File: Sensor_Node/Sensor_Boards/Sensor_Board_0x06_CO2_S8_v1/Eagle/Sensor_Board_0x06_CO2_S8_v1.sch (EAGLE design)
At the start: 16 parts, among them J1 M04_SMD_90, J3 M03_SMD_90, J4 ARDUINO_ISP, U1 SENSEAIR_S8_SMD, U2 ATMEGA328P_TQFP, Y1 8MHZ

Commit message: Removed gap between connectors to commBoard, added power jack
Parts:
- added J2: 5.5x2.1mm Barrel, wsn:POWER_JACKSMD
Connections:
- net +5V: now also J2.PWR
- net GND: now also J2.GND, J2.GNDBREAK
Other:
- note added: "ATmega328p"
- note added: "Power Jack"
- note removed: "ATmega328"
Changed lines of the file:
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@@
 <?xml version="1.0" encoding="utf-8"?>
 <!DOCTYPE eagle SYSTEM "eagle.dtd">
-<eagle version="8.2.0">
+<eagle version="8.2.2">
 <drawing>
 <settings>
@@
 <layer number="115" name="ReferenceISLANDS" color="7" fill="1" visible="yes" active="yes"/>
 <layer number="116" name="Patch_BOT" color="9" fill="4" visible="yes" active="yes"/>
+<layer number="117" name="BACKMAAT1" color="7" fill="1" visible="yes" active="yes"/>
 <layer number="118" name="Rect_Pads" color="7" fill="1" visible="yes" active="yes"/>
+<layer number="119" name="KAP_TEKEN" color="7" fill="1" visible="yes" active="yes"/>
+<layer number="120" name="KAP_MAAT1" color="7" fill="1" visible="yes" active="yes"/>
 <layer number="121" name="_tsilk" color="7" fill="1" visible="yes" active="yes"/>
 <layer number="122" name="_bsilk" color="7" fill="1" visible="yes" active="yes"/>
@@
 <layer number="128" name="_bValues" color="7" fill="1" visible="yes" active="yes"/>
 <layer number="129" name="Mask" color="7" fill="1" visible="yes" active="yes"/>
+<layer number="130" name="SMDSTROOK" color="7" fill="1" visible="yes" active="yes"/>
 <layer number="131" name="tAdjust" color="7" fill="1" visible="yes" active="yes"/>
 <layer number="132" name="bAdjust" color="7" fill="1" visible="yes" active="yes"/>
+<layer number="133" name="bottom_silk" color="7" fill="1" visible="yes" active="yes"/>
 <layer number="144" name="Drill_legend" color="7" fill="1" visible="yes" active="yes"/>
 <layer number="150" name="Notes" color="7" fill="1" visible="yes" active="yes"/>
@@
 <part name="U$16" library="myownthings" deviceset="N/C" device=""/>
 <part name="U$17" library="myownthings" deviceset="N/C" device=""/>
+<part name="J2" library="wsn" deviceset="POWER_JACK" device="SMD" value="5.5x2.1mm Barrel"/>
+<part name="P+5" library="supply1" deviceset="+5V" device=""/>
+<part name="GND4" library="SparkFun" deviceset="GND" device=""/>
 </parts>
 <sheets>
@@
 <wire x1="124.46" y1="116.84" x2="124.46" y2="203.2" width="0.1524" layer="97" style="shortdash"/>
 <wire x1="124.46" y1="203.2" x2="7.62" y2="203.2" width="0.1524" layer="97" style="shortdash"/>
-<text x="8.89" y="197.485" size="1.778" layer="97">ATmega328</text>
+<text x="8.89" y="197.485" size="1.778" layer="97">ATmega328p</text>
 <wire x1="7.62" y1="30.226" x2="7.62" y2="63.246" width="0.1524" layer="97" style="shortdash"/>
 <wire x1="7.62" y1="63.246" x2="78.74" y2="63.246" width="0.1524" layer="97" style="shortdash"/>
@@
 <text x="224.549478125" y="11.498909375" size="2.54" layer="94" font="vector">Sensor Board - CO2 (0x06)</text>
 <text x="277.911478125" y="1.133621875" size="2.54" layer="94" font="vector">1.0</text>
+<wire x1="220.98" y1="147.32" x2="132.08" y2="147.32" width="0.1524" layer="97" style="shortdash"/>
+<wire x1="220.98" y1="116.84" x2="132.08" y2="116.84" width="0.1524" layer="97" style="shortdash"/>
+<wire x1="132.08" y1="116.84" x2="132.08" y2="147.32" width="0.1524" layer="97" style="shortdash"/>
+<wire x1="220.98" y1="116.84" x2="220.98" y2="147.32" width="0.1524" layer="97" style="shortdash"/>
+<text x="134.62" y="142.24" size="1.778" layer="97">Power Jack</text>
 </plain>
 <instances>
@@
 <instance part="U$16" gate="G$1" x="108.4536375" y="172.987690625"/>
 <instance part="U$17" gate="G$1" x="108.4536375" y="175.527690625"/>
+<instance part="J2" gate="G$1" x="147.32" y="132.08"/>
+<instance part="P+5" gate="1" x="165.1" y="142.24"/>
+<instance part="GND4" gate="1" x="165.1" y="127"/>
 </instances>
 <busses>
@@
 <pinref part="S3" gate="G$1" pin="3"/>
 <wire x1="99.06" y1="88.9" x2="96.52" y2="88.9" width="0.1524" layer="91"/>
+</segment>
+<segment>
+<pinref part="J2" gate="G$1" pin="GND"/>
+<pinref part="GND4" gate="1" pin="GND"/>
+<wire x1="160.02" y1="132.08" x2="165.1" y2="132.08" width="0.1524" layer="91"/>
+<wire x1="165.1" y1="132.08" x2="165.1" y2="129.54" width="0.1524" layer="91"/>
+<pinref part="J2" gate="G$1" pin="GNDBREAK"/>
+<wire x1="160.02" y1="134.62" x2="165.1" y2="134.62" width="0.1524" layer="91"/>
+<wire x1="165.1" y1="134.62" x2="165.1" y2="132.08" width="0.1524" layer="91"/>
+<junction x="165.1" y="132.08"/>
 </segment>
 </net>
@@
 <wire x1="66.04" y1="48.26" x2="66.04" y2="53.34" width="0.1524" layer="91"/>
 </segment>
-</net>
+<segment>
+<pinref part="J2" gate="G$1" pin="PWR"/>
+<pinref part="P+5" gate="1" pin="+5V"/>
+<wire x1="160.02" y1="137.16" x2="165.1" y2="137.16" width="0.1524" layer="91"/>
+<wire x1="165.1" y1="137.16" x2="165.1" y2="139.7" width="0.1524" layer="91"/>
+</segment>
+</net>

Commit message: CO2-Board
- reset path
- some small changes
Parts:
- removed C1: 100n, eagle-ltspice:C
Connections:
- removed net N$9: C1.2, R5.1, S1.RIGHT, U2.PC6(/RESET)
- removed net VCC: C9.1, U2.AVCC, U2.VCC@4, U2.VCC@6
- net +3V3: now also C9.1, U2.AVCC, U2.VCC@4, U2.VCC@6
- net RESET: now also R5.1, S1.RIGHT, U2.PC6(/RESET); no longer C1.1

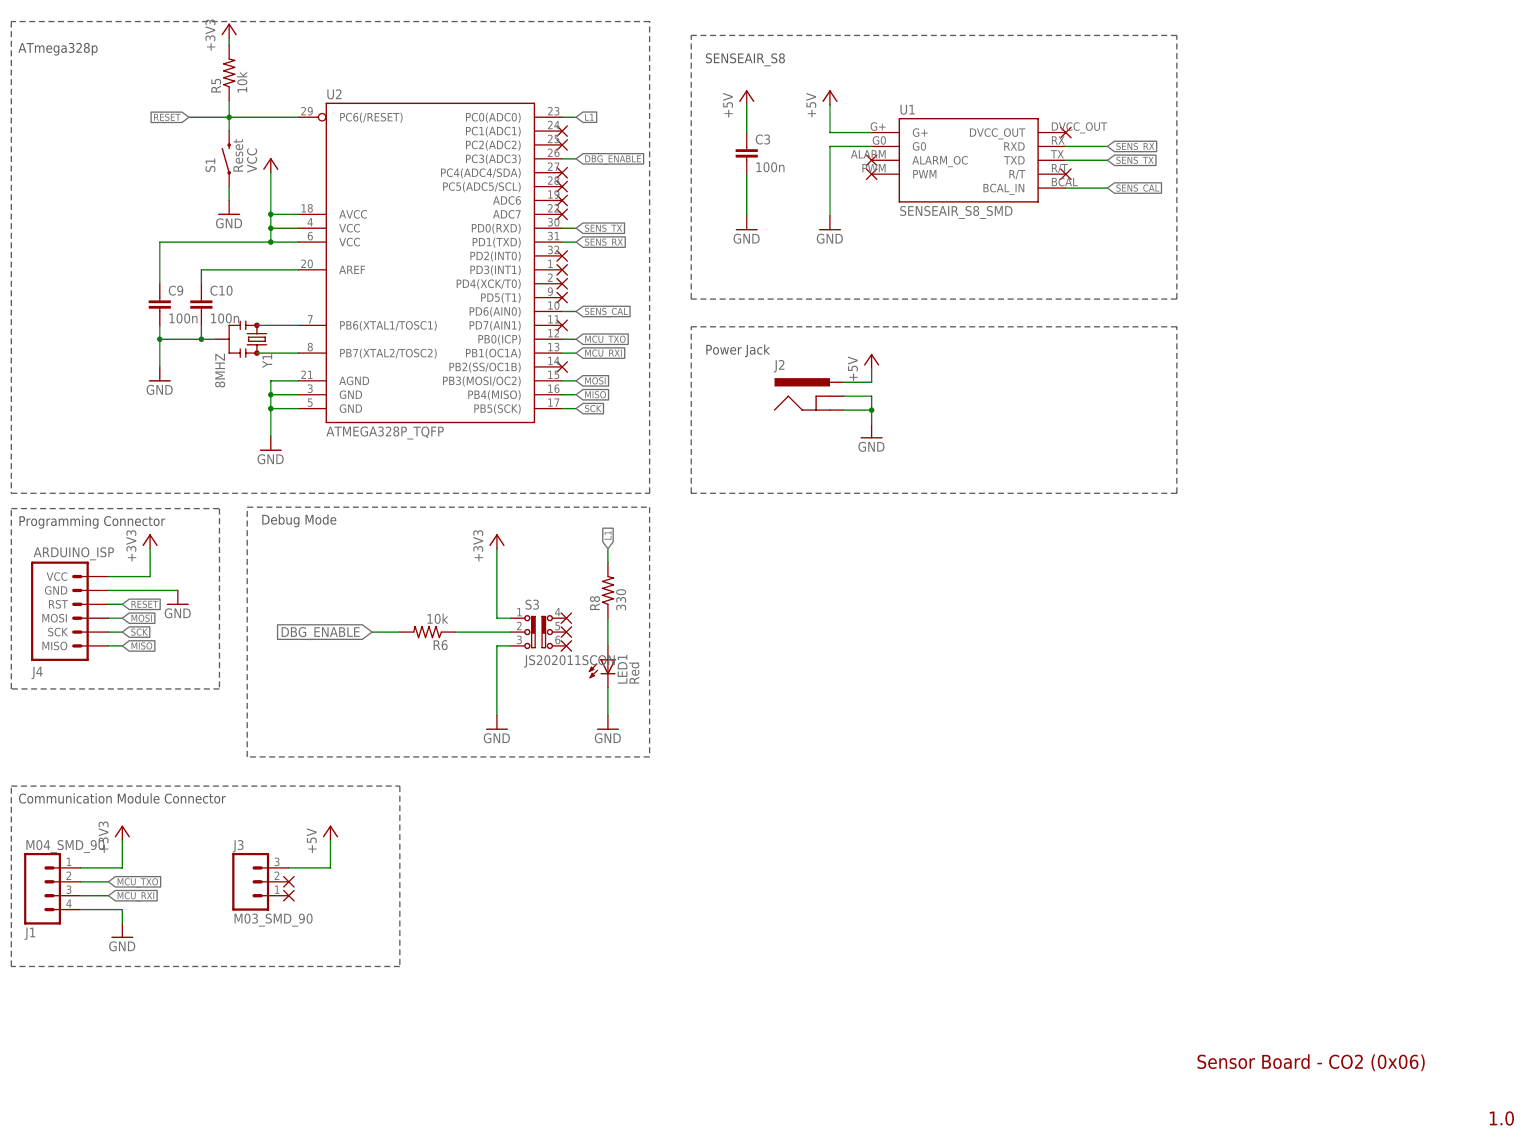
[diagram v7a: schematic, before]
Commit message: Finished SHT31 and CO2-Board
- finished tidying SHT31
- added FTDI-connector to CO2-Sensorboard
- tidied CO2-Sensorboard
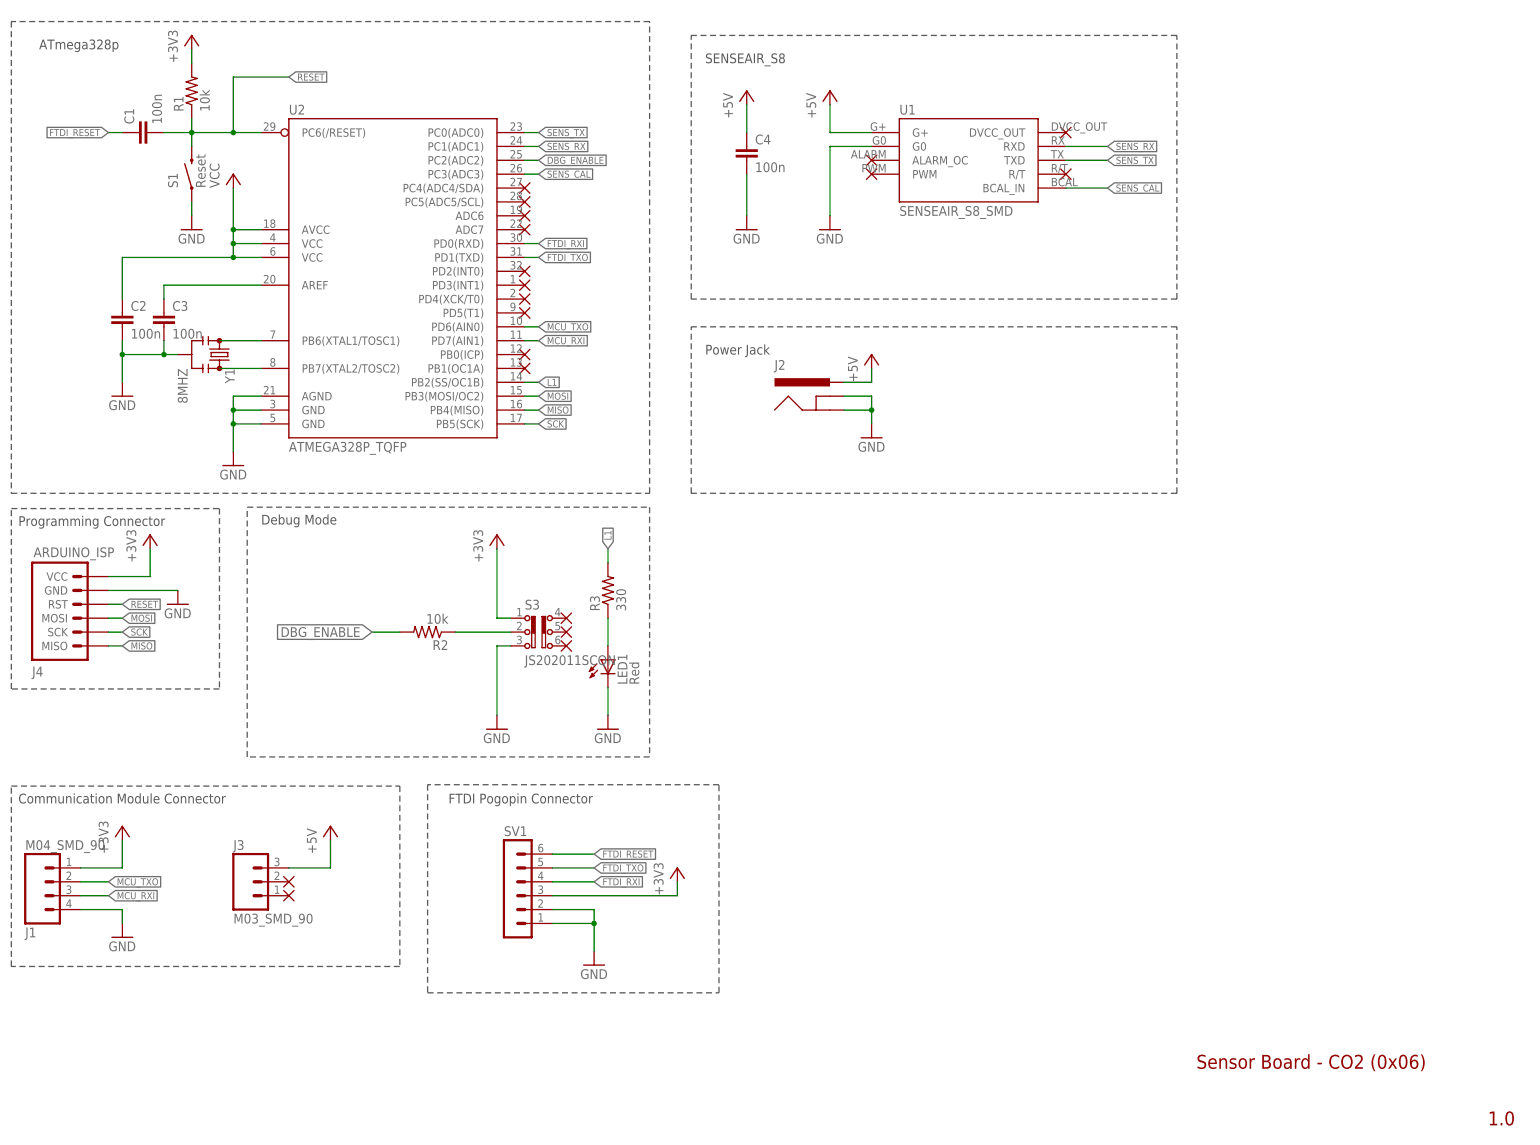
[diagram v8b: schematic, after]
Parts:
- removed C10, C9: 100n, eagle-ltspice:C
- removed R5: 10k, SparkFun-Passives:RESISTOR0805-RES
- added C1, C2, C4: 100n, eagle-ltspice:C
- added R1: 10k, SparkFun-Passives:RESISTOR0805-RES
- added SV1: (no value), con-lstb:MA06-1
- renumbered R6 to R2, R8 to R3
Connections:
- new net FTDI_RESET: C1.1, SV1.6
- new net FTDI_RXI: SV1.4, U2.PD0(RXD)
- new net FTDI_TXO: SV1.5, U2.PD1(TXD)
- net +3V3: now also C2.1, R1.2, SV1.3; no longer C9.1, R5.2
- net +5V: now also C4.1; no longer C3.1
- net DBG_ENABLE: now also U2.PC2(ADC2); no longer U2.PC3(ADC3)
- net GND: now also C2.2, C4.2, SV1.1, SV1.2; no longer C10.2, C9.2
- net L1: now also U2.PB2(SS/OC1B); no longer U2.PC0(ADC0)
- net MCU_RXI: now also U2.PD7(AIN1); no longer U2.PB1(OC1A)
- net MCU_TXO: now also U2.PD6(AIN0); no longer U2.PB0(ICP)
- net N$15: now also C3.1; no longer C10.1
- net RESET: now also C1.2, R1.1; no longer R5.1
- net SENS_CAL: now also U2.PC3(ADC3); no longer U2.PD6(AIN0)
- net SENS_RX: now also U2.PC1(ADC1); no longer U2.PD1(TXD)
- net SENS_TX: now also U2.PC0(ADC0); no longer U2.PD0(RXD)
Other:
- note added: "FTDI Pogopin Connector"
- moved on the sheet: C3, S1, U2, Y1
